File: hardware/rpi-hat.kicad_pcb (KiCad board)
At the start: 2 copper layers, 65 x 56 mm, 75 parts, among them J1 Conn_02x20_Odd_Even__Rpi, J10 A1, J11 A2, J12 A3, J13 A4, J14 A5, J15 Conn_01x01_Male, J16 Conn_01x02_Male, J17 Fan 1, J18 Fan 2, J2 USART, J3 I2C 3.3V, J4 I2C 3.3V, J5 I2C 5V, J6 PPS, J7 10103594-0001LF, J8 Jumper, J9 A0, U1 Fan Driver, U2 EEPROM, U3 Buffer, U4 BSS138, U5 BSS138, U6 Buffer, U7 DAC, U8 Multiplexor, U9 ADC

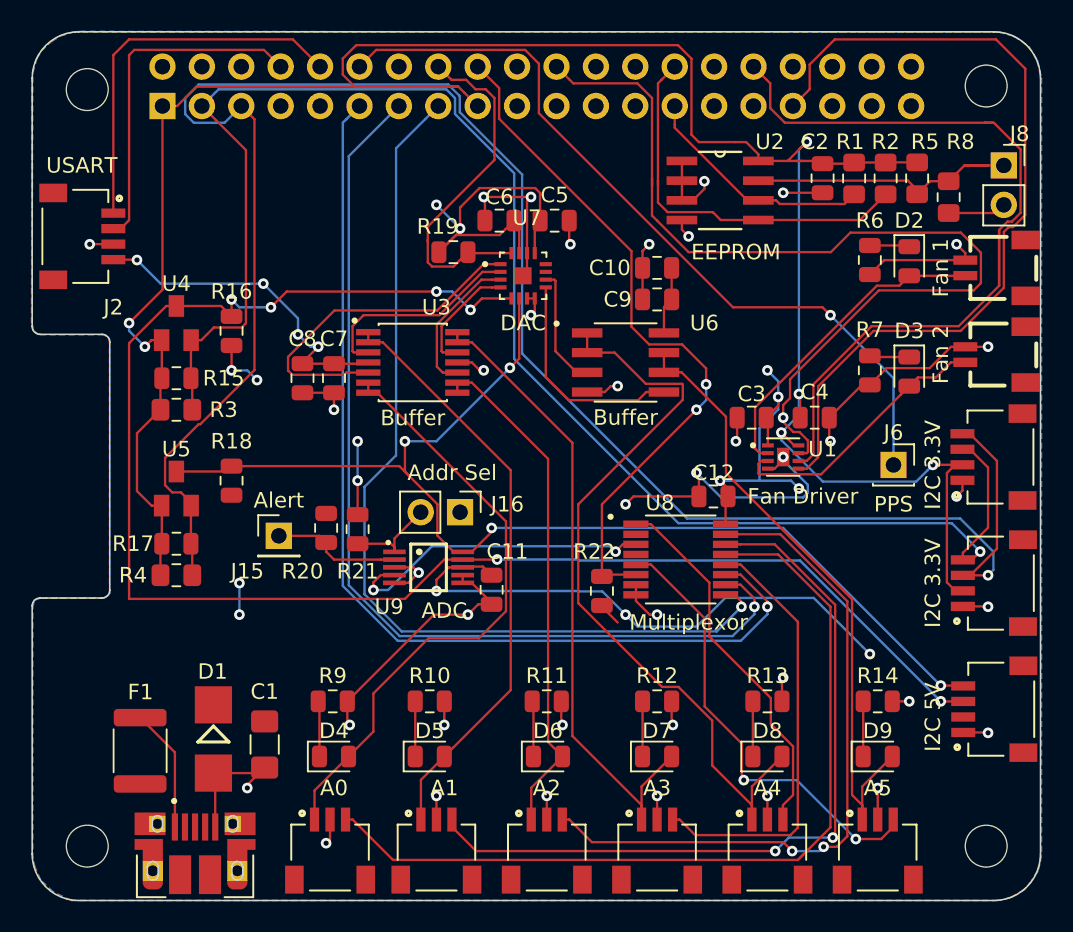
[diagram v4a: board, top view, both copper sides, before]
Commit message: Add Voltage Regulator.  Update traces.
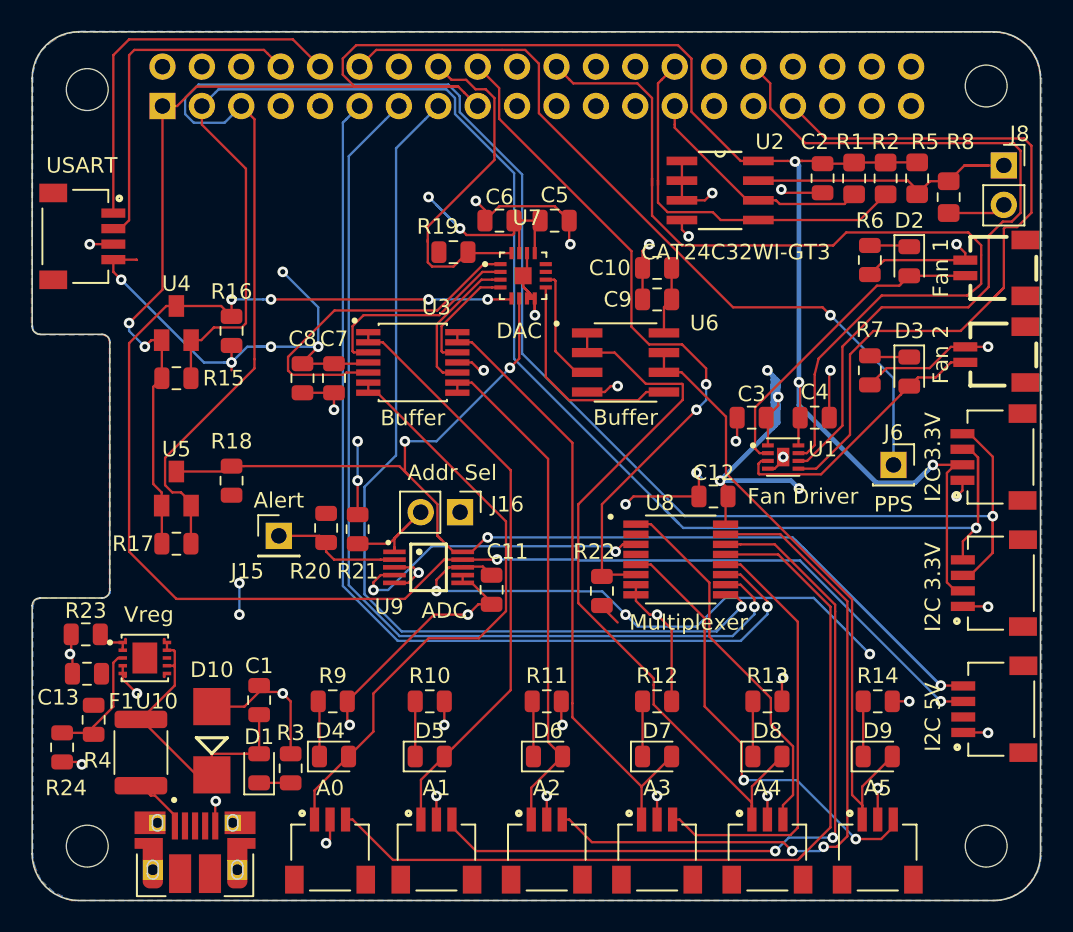
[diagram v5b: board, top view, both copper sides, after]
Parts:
- added C13: 47uF, Capacitor_SMD:C_0805_2012Metric, F.Cu at (203.5, 135.4)
- added D10: SMBJ5.0A, zephyrus-iaq:SMBJ5.0A, F.Cu at (211.6, 139.7)
- added R23: 100k, Resistor_SMD:R_0805_2012Metric, F.Cu at (203.5, 132.8)
- added R24: 1k, Resistor_SMD:R_0805_2012Metric, F.Cu at (201.9, 140.1)
- added U10: Vreg, zephyrus-iaq:REG_EY1501DI-ADJ, F.Cu at (207.3, 134.4)
- C1: footprint Resistor_SMD:R_1206_3216Metric_Pad1.42x1.75mm_HandSolder -> Capacitor_SMD:C_0805_2012Metric
- D1: value SMBJ5.0A -> PWR; footprint zephyrus-iaq:SMBJ5.0A -> Diode_SMD:D_0805_2012Metric
- Fan 1: renamed from J17; value Fan 1 -> SM02B-SRSS-TB(LF)(SN)
- Fan 2: renamed from J18; value Fan 2 -> SM02B-SRSS-TB(LF)(SN)
- J3, J4: footprint SM04B-SRSS-TB_LF__SN_:JST_SM04B-SRSS-TB(LF)(SN) -> zephyrus-iaq:JST_SM04B-SRSS-TB(LF)(SN)
- J7: footprint 10103594-0001LF:FCI_10103594-0001LF -> zephyrus-iaq:FCI_10103594-0001LF
- R3: value 10k -> 330; footprint Resistor_SMD:R_0805_2012Metric_Pad1.15x1.40mm_HandSolder -> Resistor_SMD:R_0805_2012Metric
- R4: value 10k -> 2.61k; footprint Resistor_SMD:R_0805_2012Metric_Pad1.15x1.40mm_HandSolder -> Resistor_SMD:R_0805_2012Metric
- U2: value EEPROM -> CAT24C32WI-GT3
- U8: value Multiplexor -> Multiplexer
- moved R3 24.3 mm to (216.7, 141.5), turned to 90 degrees
- moved R4 10.7 mm to (204.0, 138.4), turned to 270 degrees
- moved D1 3.50 mm to (214.6, 141.5), turned to 90 degrees
- moved C1 2.88 mm to (214.6, 137.1), turned to 90 degrees
- moved F1 0.12 mm to (207.0, 140.5), turned to 90 degrees
- moved J7 0.07 mm to (210.5, 148.0)
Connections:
- C1 pad 1: +5V -> /PowerManagement/VREG_IN_5V
- D1 pad 1: +5V -> Net-(D1-Pad1)
- D1 pad 2: GND -> /PowerManagement/VREG_IN_5V
- F1 pad 2: +5V -> /PowerManagement/VREG_IN_5V
- R3 pad 1: +3V3 -> Net-(D1-Pad1)
- R3 pad 2: /GPIO2(SDA1) -> GND
- R4 pad 1: +3V3 -> +5V
- R4 pad 2: /GPIO3(SCL1) -> /PowerManagement/VREG_SENSE
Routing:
- net /PowerManagement/VREG_IN_5V: track 0.00 -> 19.4 mm
- net /SCL_5: track 75.2 -> 88.5 mm
- net +5V: track 117.2 -> 129.8 mm, vias 19 -> 18
- net /PowerManagement/VREG_SENSE: track 0.00 -> 7.95 mm
- net +3V3: track 157.3 -> 149.5 mm, vias 6 -> 5
- net GND: track 133.1 -> 138.6 mm, vias 38 -> 40
- net /FAN_PWM1: track 54.1 -> 49.1 mm
- net /GPIO3(SCL1): track 126.6 -> 122.1 mm
- net /FAN_PWM0: track 54.3 -> 50.3 mm
- net Net-(F1-Pad1): track 7.98 -> 4.34 mm
- net /SDA_5: track 103.5 -> 100.4 mm
- net /ADC_Subsystem/ADC_ADDR: track 6.02 -> 8.88 mm
- net /Analog_Sensors/BUF_OUT_3: track 41.7 -> 39.6 mm
- net Net-(D1-Pad1): track 0.00 -> 2.03 mm
- net /FAN_nSLEEP: track 61.5 -> 59.6 mm, vias 1 -> 0
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
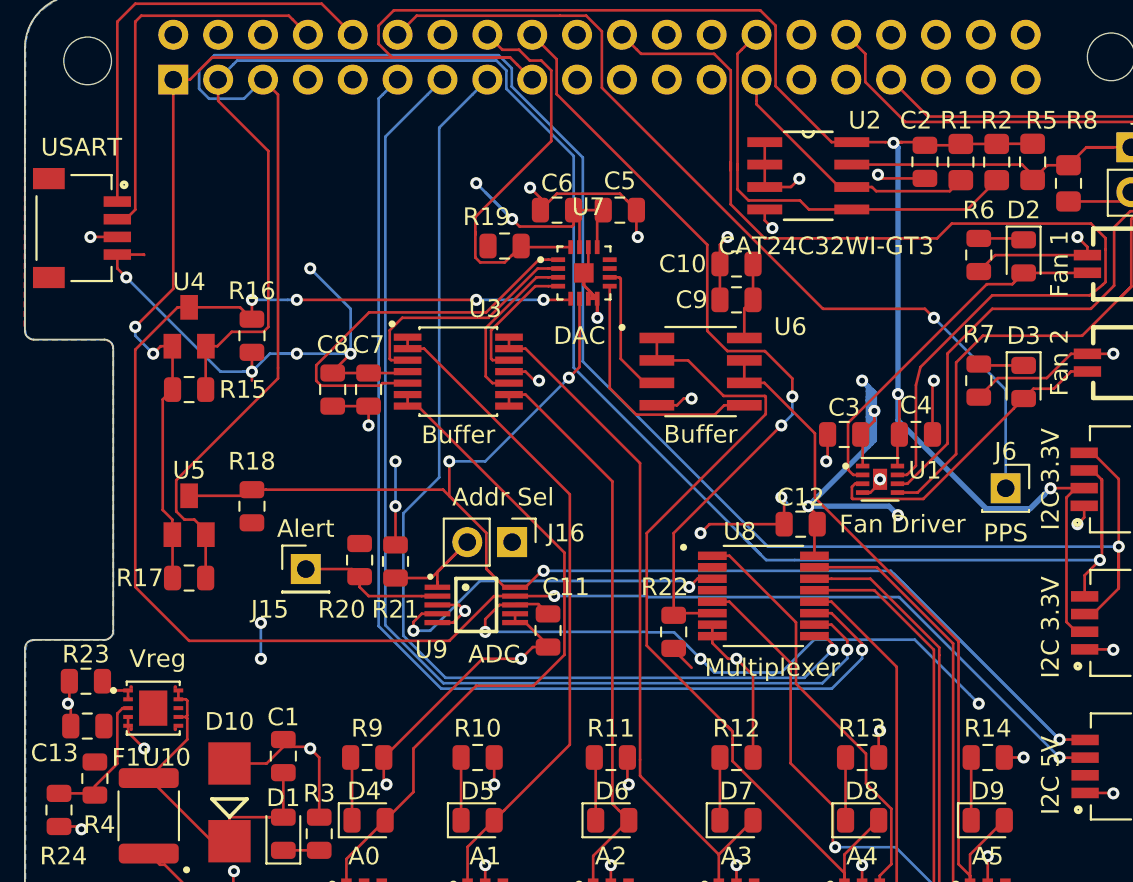
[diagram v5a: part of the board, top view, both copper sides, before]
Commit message: Update PCB Logo
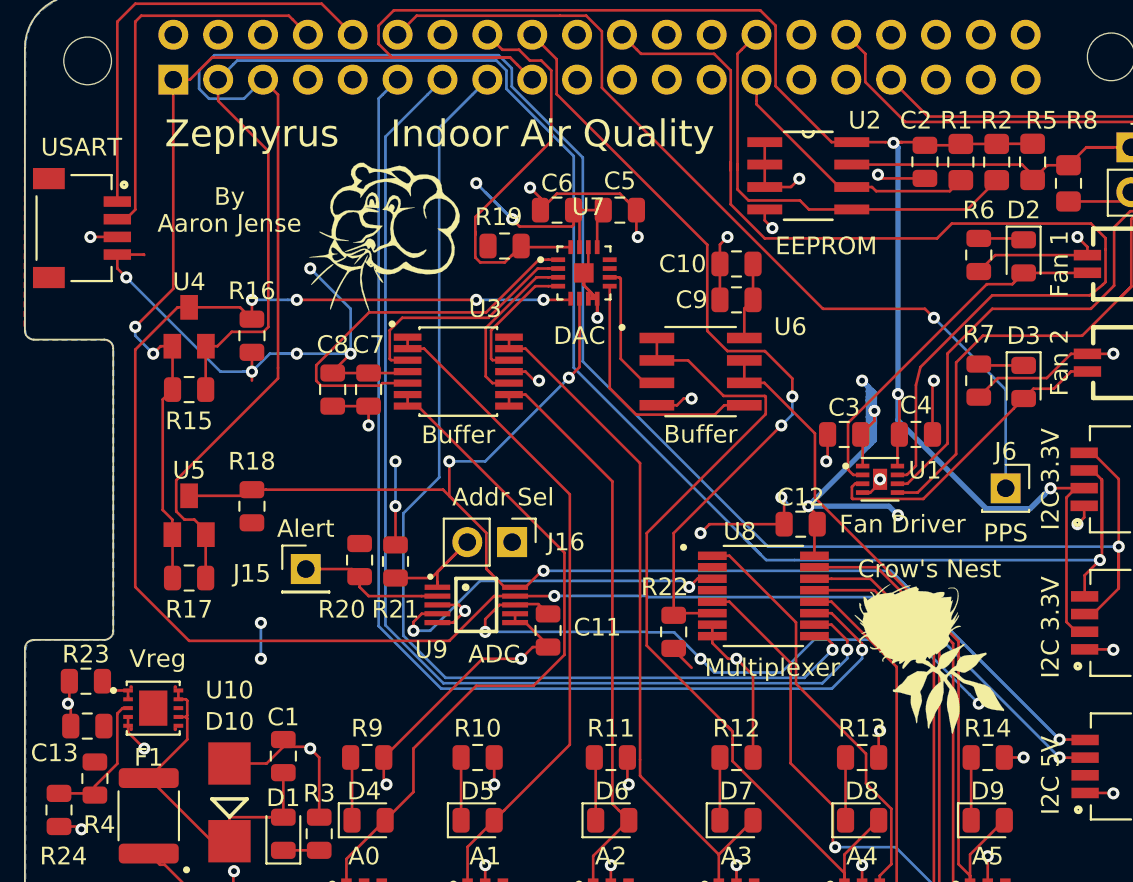
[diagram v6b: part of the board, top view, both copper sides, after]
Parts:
- added G***: LOGO, zephyrus-iaq:CC-license, F.Cu at (209.3, 135.9)
- added G***: LOGO, zephyrus-iaq:crow-fly, F.Cu at (232.7, 109.2)
- added G***: LOGO, zephyrus-iaq:wind-lineart_25mm_24mm, B.Cu at (205.7, 109.0)
- added G***: LOGO, zephyrus-iaq:crows-nest-25mm_25mm, F.Cu at (252.2, 134.6)
- added G***: LOGO, zephyrus-iaq:wind-lineart, F.Cu at (220.2, 107.7)
- added G***: Crow's Nest, zephyrus-iaq:crows-nest, F.Cu at (251.2, 131.6)
- U2: value CAT24C32WI-GT3 -> EEPROM
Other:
- board text added: "A Crow's Nest Project."
- board text added: "Aaron Jense"
- board text added: "Amy & Dennis Heidner"
- board text added: "By"
- board text added: "Capstone Project, 12/2019"
- board text added: "Created by Aaron Jense"
- board text added: "Electrical & Computer Engineering"
- board text added: "Indoor Air Quality"
- board text added: "Indoor Air Quality Logger"
- board text added: "Montana State University"
- board text added: "Sponsored By:"
- board text added: "Team Members: Aaron Jense Anthony Ciccotosto Justin Smith Benjamin Seal"
- board text added: "The Rextor Group PLLC"
- board text added: "Zephyrus"

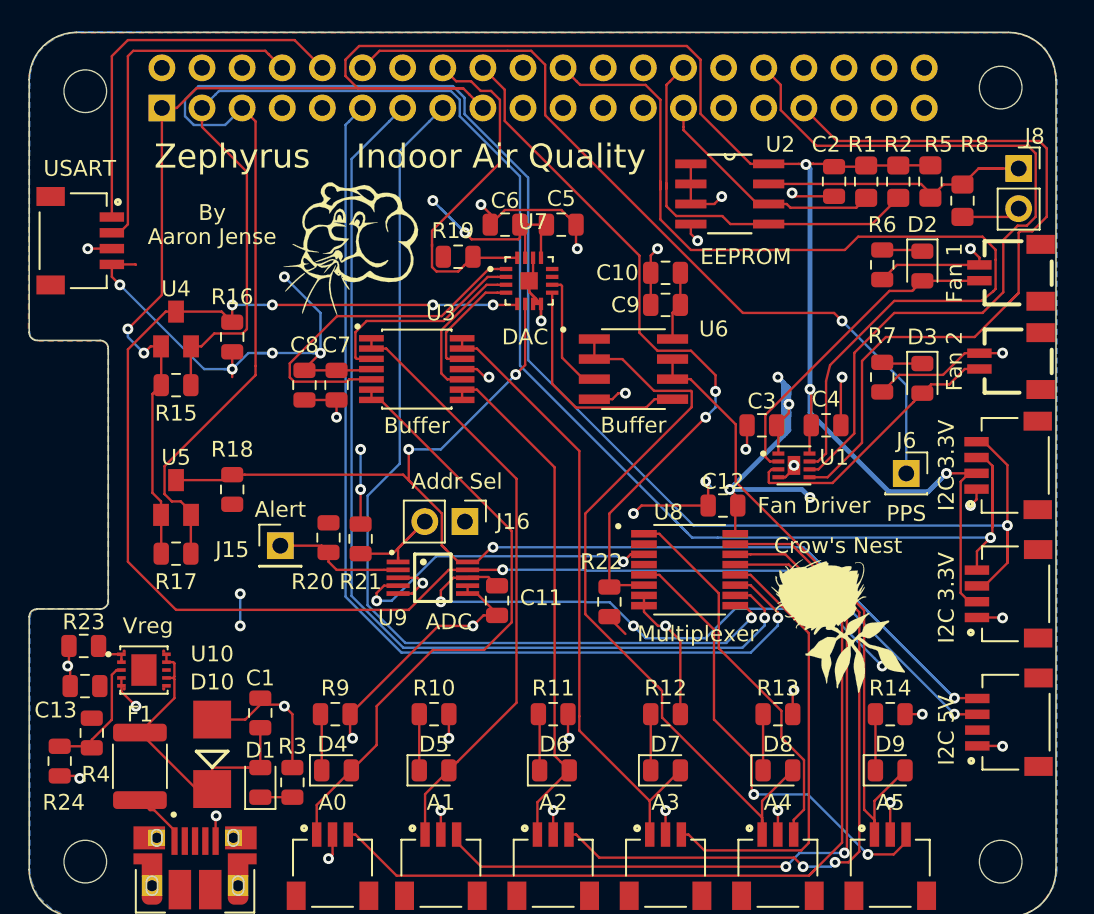
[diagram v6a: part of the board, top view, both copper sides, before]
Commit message: Fixed EEPROM I2C.  Removed uneeded pull up resistors.
Rpi has internal pull ups.
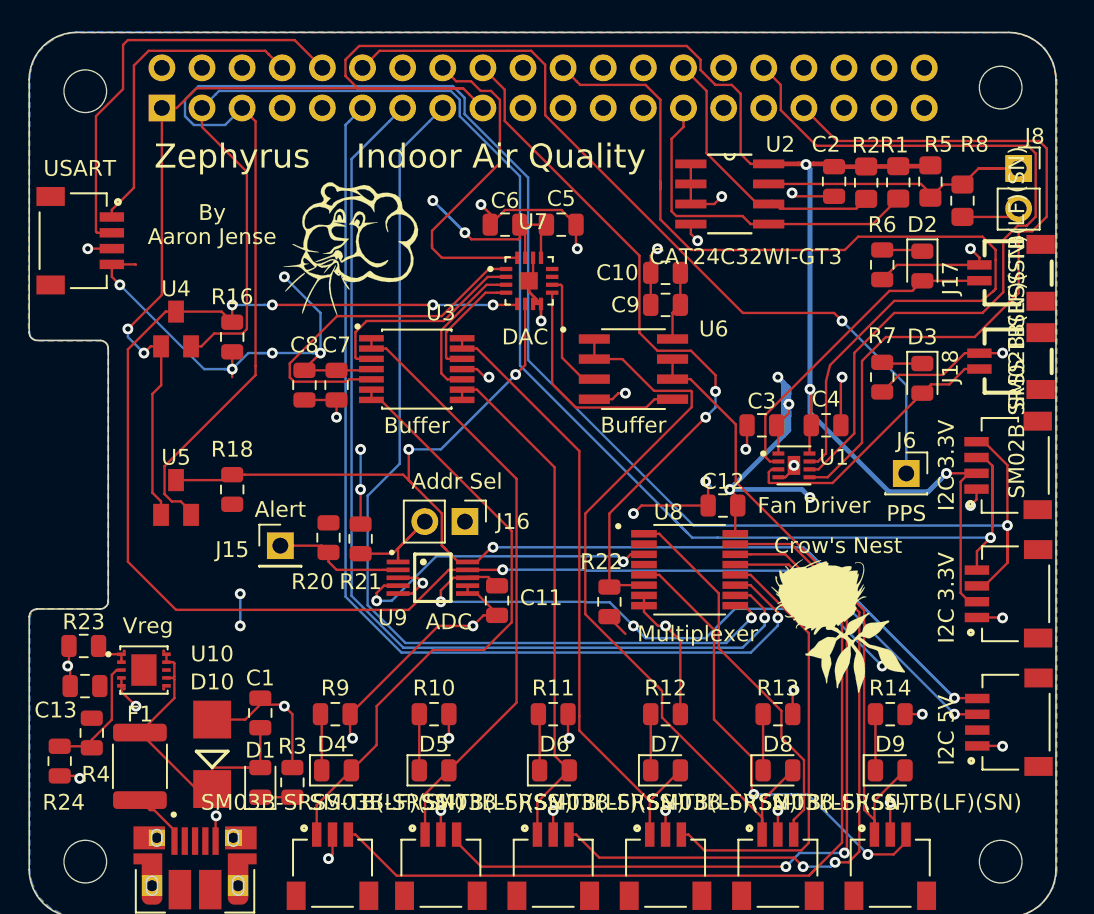
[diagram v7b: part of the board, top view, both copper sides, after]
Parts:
- removed R15, R17: 10k, Resistor_SMD:R_0805_2012Metric
- removed R19: 10K, Resistor_SMD:R_0805_2012Metric
- J10: value A1 -> SM03B-SRSS-TB(LF)(SN)
- J11: value A2 -> SM03B-SRSS-TB(LF)(SN)
- J12: value A3 -> SM03B-SRSS-TB(LF)(SN)
- J13: value A4 -> SM03B-SRSS-TB(LF)(SN)
- J14: value A5 -> SM03B-SRSS-TB(LF)(SN)
- J17: renamed from Fan 1
- J18: renamed from Fan 2
- J9: value A0 -> SM03B-SRSS-TB(LF)(SN)
- R16, R18: value 10k -> 1.8k
- R5: value 10k -> 1k
- U2: value EEPROM -> CAT24C32WI-GT3
- moved R2 2.03 mm to (253.0, 103.5)
- moved R1 2.03 mm to (255.0, 103.5)
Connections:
- J2 pad 1: /GPIO15(RXD0) -> /GPIO14(TXD0)
- J2 pad 2: /GPIO14(TXD0) -> /GPIO15(RXD0)
- U2 pad 5: /ID_SC_EEPROM -> /ID_SD_EEPROM
- U2 pad 6: /ID_SD_EEPROM -> /ID_SC_EEPROM
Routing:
- net /ID_SC_EEPROM: track 24.9 -> 17.7 mm
- net /ID_SD_EEPROM: track 15.3 -> 22.3 mm
- net /GPIO15(RXD0): track 24.7 -> 27.5 mm
- net /GPIO2(SDA1): track 105.4 -> 102.9 mm
- net /GPIO3(SCL1): track 122.1 -> 119.6 mm
- net /GPIO14(TXD0): track 22.2 -> 20.4 mm
- net +3V3: track 149.5 -> 148.0 mm
- net /DAC_CLR_pu: track 22.9 -> 21.4 mm
